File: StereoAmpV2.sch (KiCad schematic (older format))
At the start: 10 parts, among them J1 Conn_01x07_Male, J2 Screw_Terminal_01x02, J3 Screw_Terminal_01x02, U1 MAX98357AETE+T, U2 MAX98357AETE+T

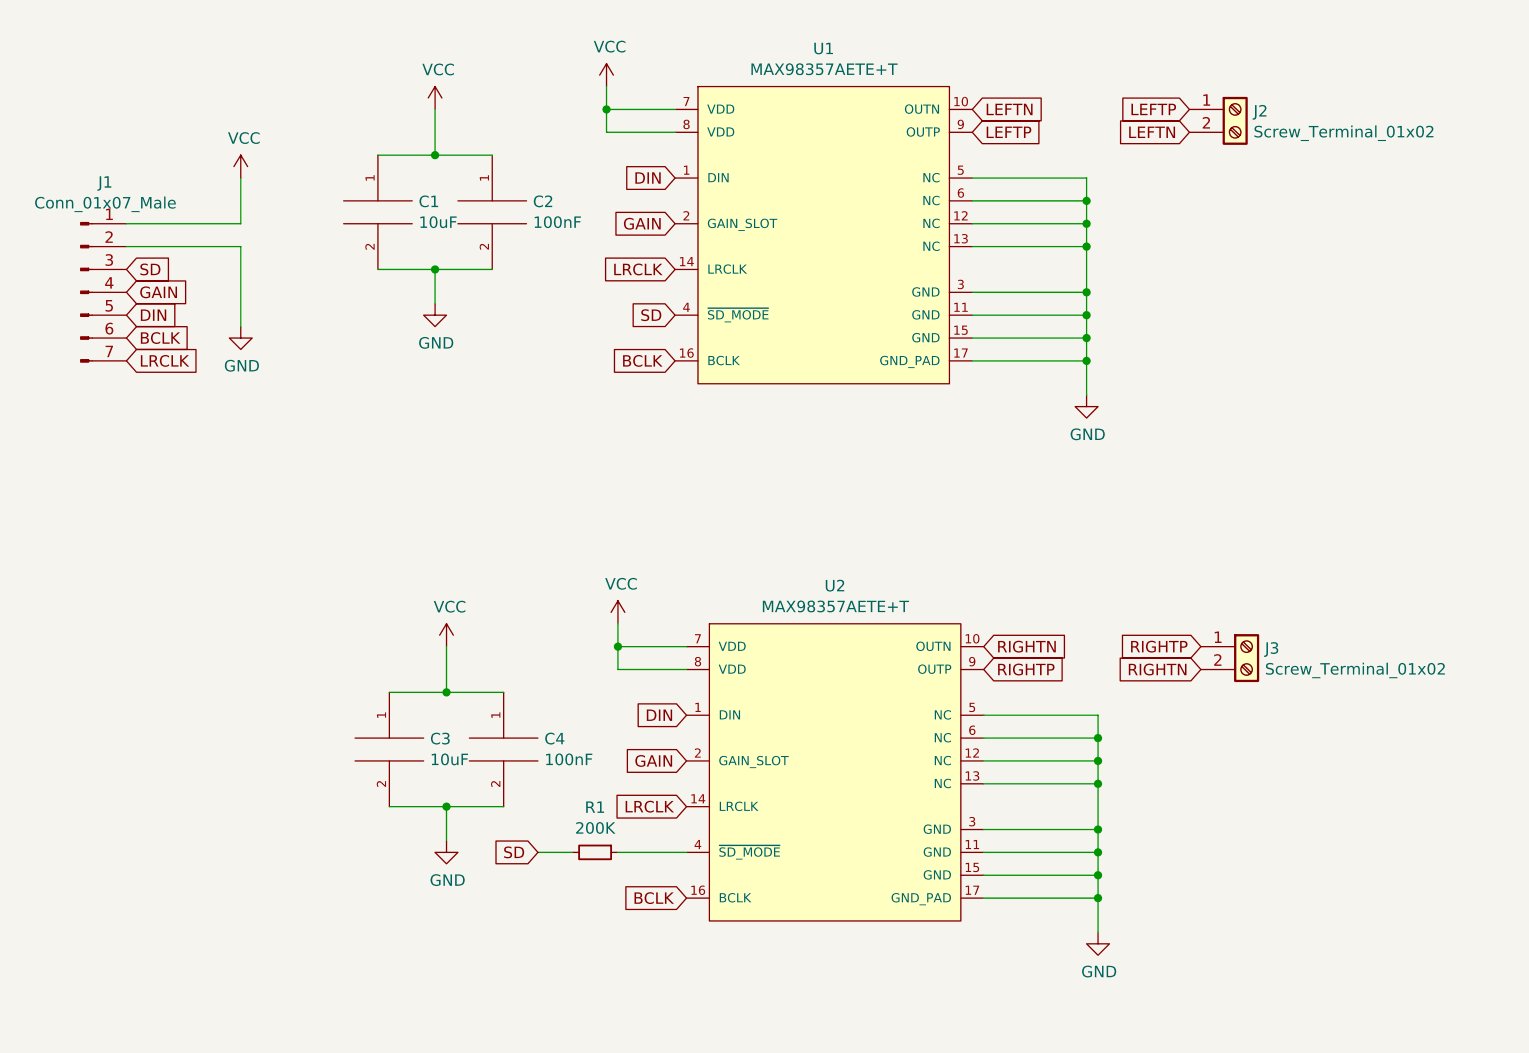
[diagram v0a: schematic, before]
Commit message: Adds some boxes and labels to schematic
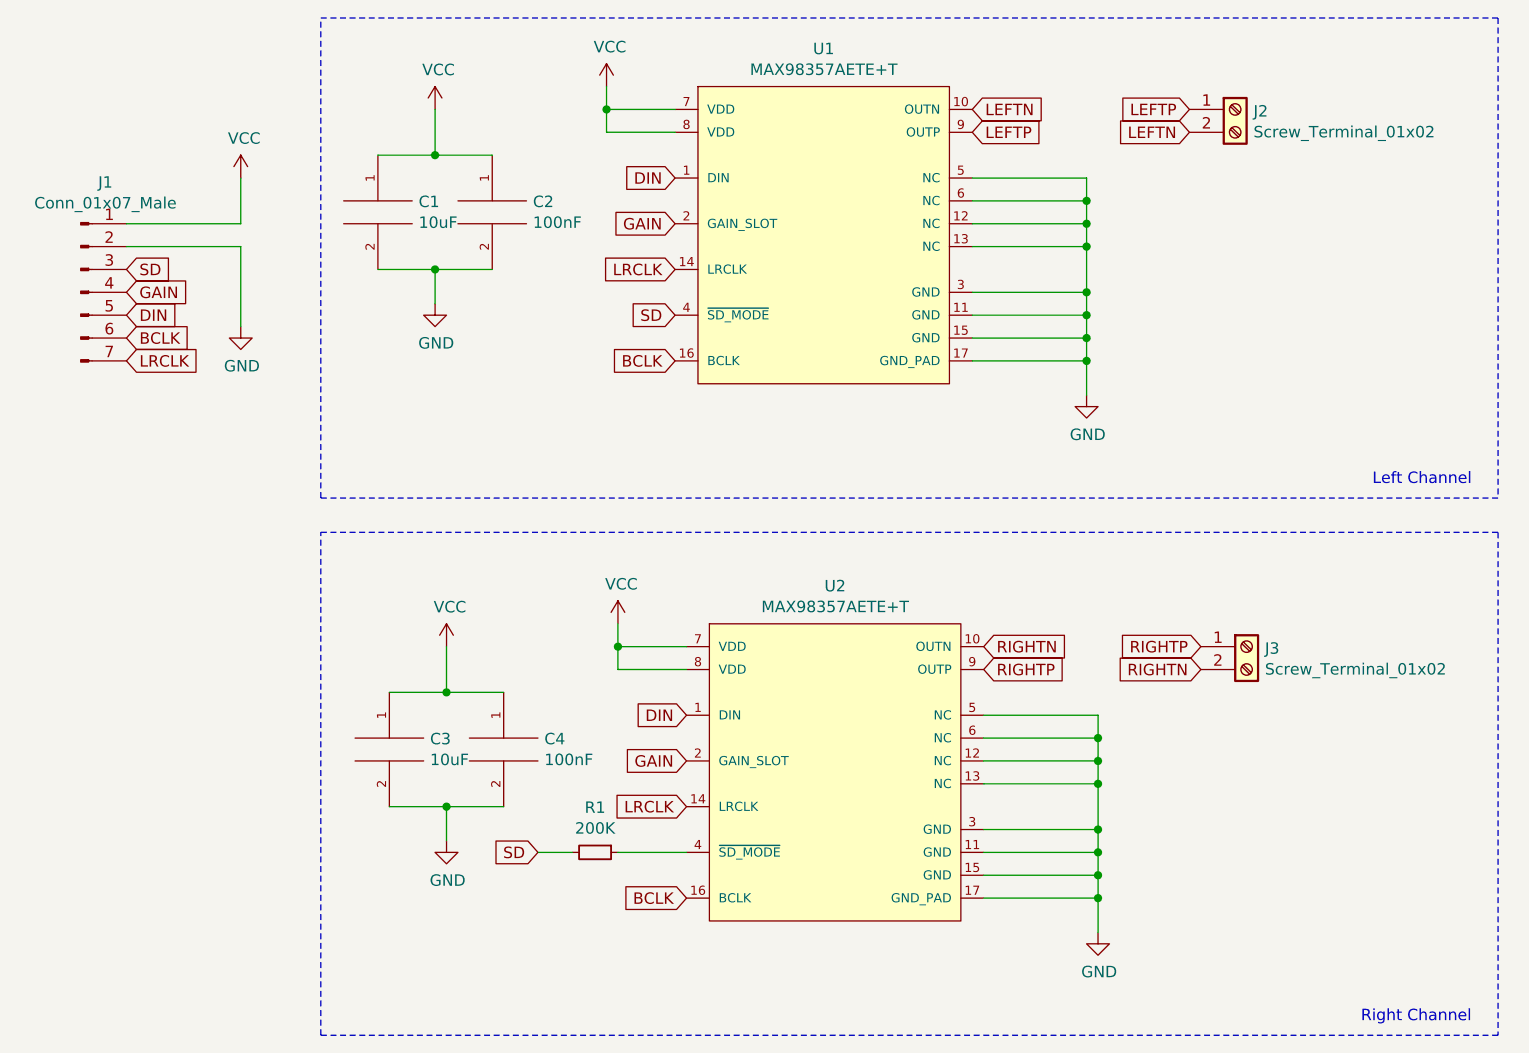
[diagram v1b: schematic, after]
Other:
- note added: "Left Channel"
- note added: "Right Channel"
